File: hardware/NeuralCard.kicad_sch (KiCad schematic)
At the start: 54 parts, among them J1 ProgPads, SW1 SW_PUSH, SW2 SW_PUSH, SW3 MSK12C02, U1 ESP32-S3-WROOM-1, U2 LSM6DS3TR-C, U4 ST25DV04KC-IE6S3

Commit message: feat: usb-c dual power
Implement the dual-power topology the generator's power section always
promised: USB-C + coin cell with P-FET auto source selection.

New parts (all LCSC-verified): J2 TYPE-C-31-M-12 (C165948) with 5.1k Rd
on CC1/CC2 (R7/R8, C23186) so any source grants 5V; U5 USBLC6-2SC6
(C7519) ESD array on the native-USB data lines; U3 ME6211C33M5G-N LDO
(C82942) VBUS->+3V3 with CE tied to VIN and 1uF on VIN/VOUT (C6/C7,
C15849); Q1 AO3401A (C15127) battery-path P-FET with 100k gate pulldown
(R13, C25803 same part as R14). USB_DP/USB_DM now land on U1 pins 14/13
(IO20/IO19, the S3's native USB).

SW3 rewiring: the switch throw (pin 3) used to drive +3V3 directly; it
now feeds new net VBAT_SW, the source of Q1. Drain lands on +3V3, gate
on VBUS: USB present holds the gate high and isolates the coin (body
diode stays off, 3.3V drain vs 3.0V source < Vf); USB absent, R13 pulls
the gate low and the coin feeds the rail. Pole/throw roles unchanged.
The PCB still has +3V3 on SW3 pad 3 until the next board update, which
will also place the new footprints (deliberately not done here).

All three PWR_FLAGs removed: every power net now has a real power_out
driver (BT1 for GND/VBAT, J2 for VBUS, U3 VOUT for +3V3), so the flags
were the source of the two pre-existing ERC pin_to_pin errors. J2's
duplicate VBUS pin B4A9 retyped power_out->passive in JLC.kicad_sym to
avoid a self-collision with A4B9 (standard twin-power-pin practice).
ERC: was 2 errors + 1 warning, now 0 errors + 1 warning (the
pre-existing, intentional U2 SDO/SA0 address-strap-to-rail warning).
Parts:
- added C6, C7: 1uF, Capacitor_SMD:C_0603_1608Metric, symbol Device:C
- added J2: TYPE-C-31-M-12, JLC:USB-C_SMD-TYPE-C-31-M-12_1, symbol JLC:TYPE-C-31-M-12
- added Q1: AO3401A, JLC:SOT-23_L2.9-W1.3-P1.90-LS2.4-BR, symbol JLC:AO3401A
- added R13: 100k, Resistor_SMD:R_0603_1608Metric, symbol Device:R
- added R7, R8: 5.1k, Resistor_SMD:R_0603_1608Metric, symbol Device:R
- added U3: ME6211C33M5G-N, JLC:SOT-23-5_L3.0-W1.7-P0.95-LS2.8-BL, symbol JLC:ME6211C33M5G-N
- added U5: USBLC6-2SC6, JLC:SOT-23-6_L2.9-W1.6-P0.95-LS2.8-BL, symbol JLC:USBLC6-2SC6
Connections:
- net +3V3: now also C7.1, Q1.3 (D), U3.5 (VOUT); no longer SW3.3 (C)
- net GND: now also C6.2, C7.2, J2.1 (EH), J2.2 (EH), J2.3 (EH), J2.4 (EH), J2.A1B12 (GND), J2.B1A12 (GND), R13.2, R7.2, R8.2, U3.2 (VSS), U5.2
- net USB_DM: now reaches U1.13 (IO19)
- net USB_DM: now also J2.A7 (DN1), J2.B7 (DN2), U5.3, U5.4
- net USB_DP: now reaches U1.14 (IO20)
- net USB_DP: now also J2.A6 (DP1), J2.B6 (DP2), U5.1, U5.6
- new net CC1: J2.A5 (CC1), R7.1
- new net CC2: J2.B5 (CC2), R8.1
- new net VBAT_SW: Q1.2 (S), SW3.3 (C)
- new net VBUS: C6.1, J2.A4B9 (VBUS), J2.B4A9 (VBUS), Q1.1 (G), R13.1, U3.1 (VIN), U3.3 (CE), U5.5
- no-connect marks 30 -> 31
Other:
- note added: "POWER (CR2032 coin -> SW3 -> VBAT_SW -> Q1 P-FET -> 3V3 rail)"
- note added: "USB-C (VBUS -> ME6211 3.3V LDO; Q1 P-FET isolates coin when USB present; USBLC6 ESD)"
- note removed: "POWER (CR2032 coin -> SW3 -> 3V3 rail; also fed by prog-pad 3V3)"

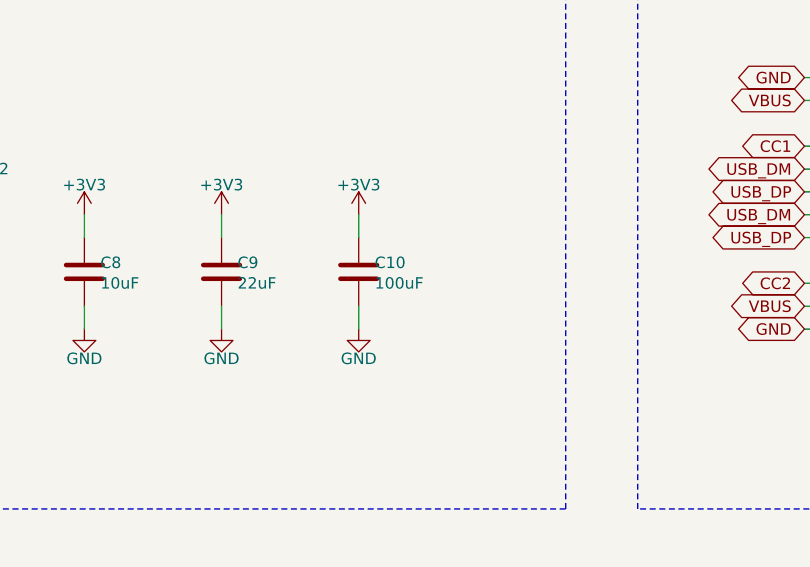
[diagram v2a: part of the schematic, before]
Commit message: fix c10 value
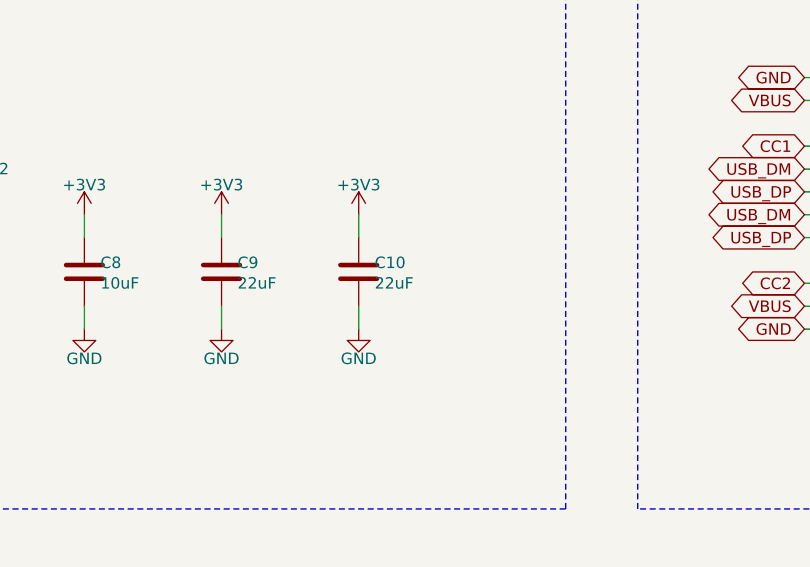
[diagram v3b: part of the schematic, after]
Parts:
- C10: value 100uF -> 22uF
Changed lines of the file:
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@@
 			)
 		)
-		(property "Value" "100uF"
+		(property "Value" "22uF"
 			(at 128.778 74.92999999999999 0)
 			(effects
